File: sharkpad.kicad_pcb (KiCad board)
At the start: 2 copper layers, 89.8 x 19.3 mm, 7 parts, among them SW1 SW_Push, SW2 SW_Push, SW3 SW_Push, SW4 SW_Push, U1 MOUDLE-SEEEDUINO-XIAO

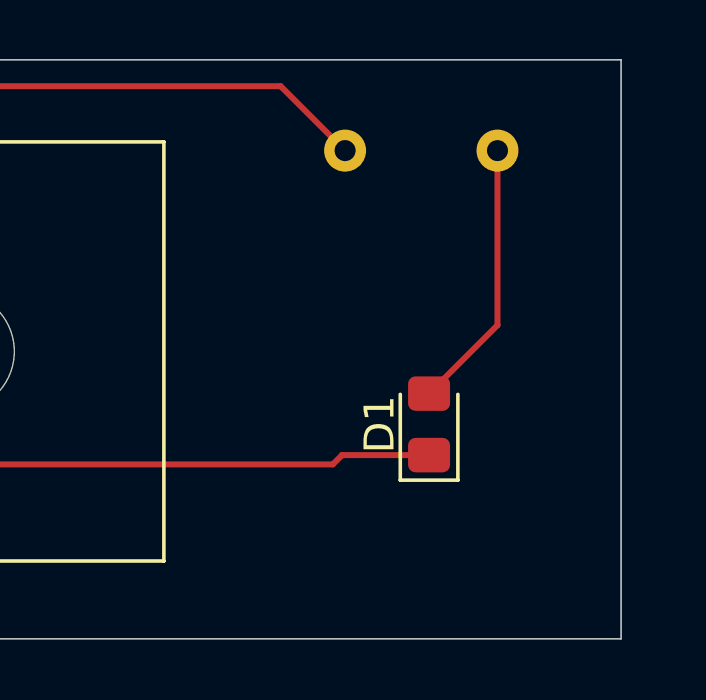
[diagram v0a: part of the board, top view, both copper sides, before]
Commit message: add BOM
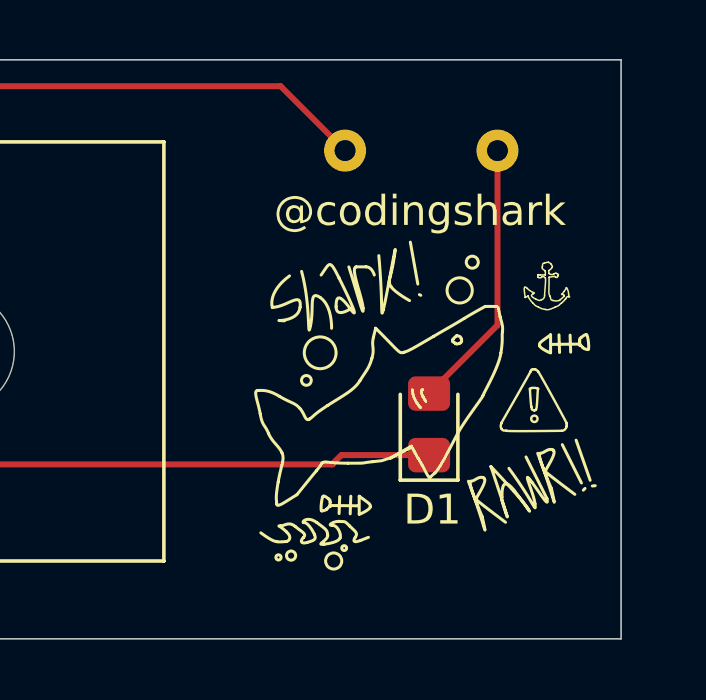
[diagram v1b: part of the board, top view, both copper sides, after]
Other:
- board text added: "@codingshark"
